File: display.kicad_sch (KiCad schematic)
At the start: 40 parts, among them J301 ConnectorLCDFrontLight, J302 FPC24(0.5MM), J303 FPC10(0.5MM), Q301 2N7002, Q302 2N7002, Q303 AO3401A

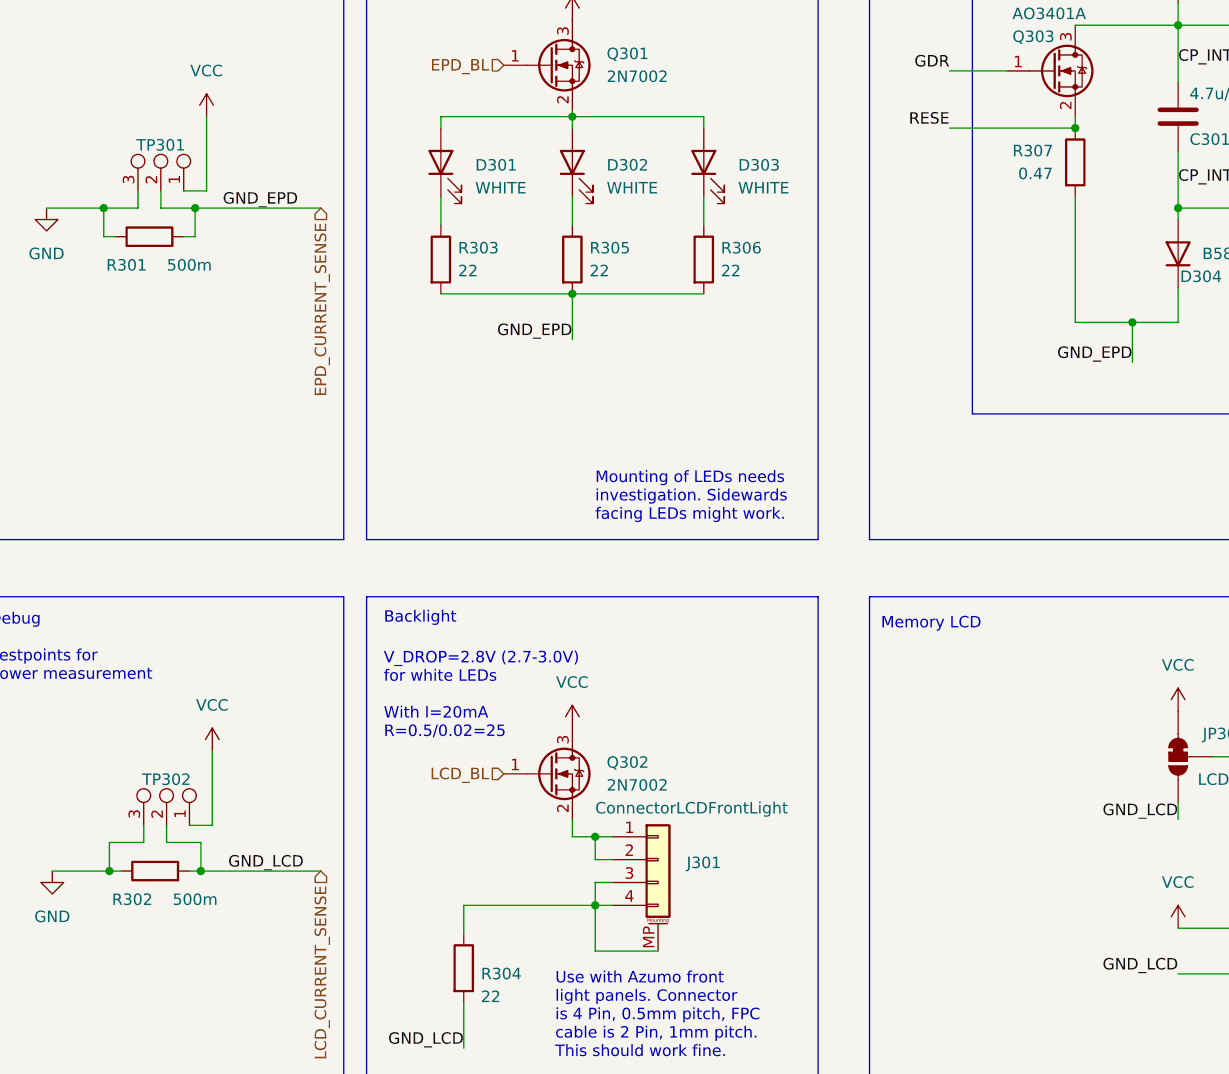
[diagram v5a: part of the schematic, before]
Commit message: Schematic: BOM consolidation and JLCPCB part no annotation
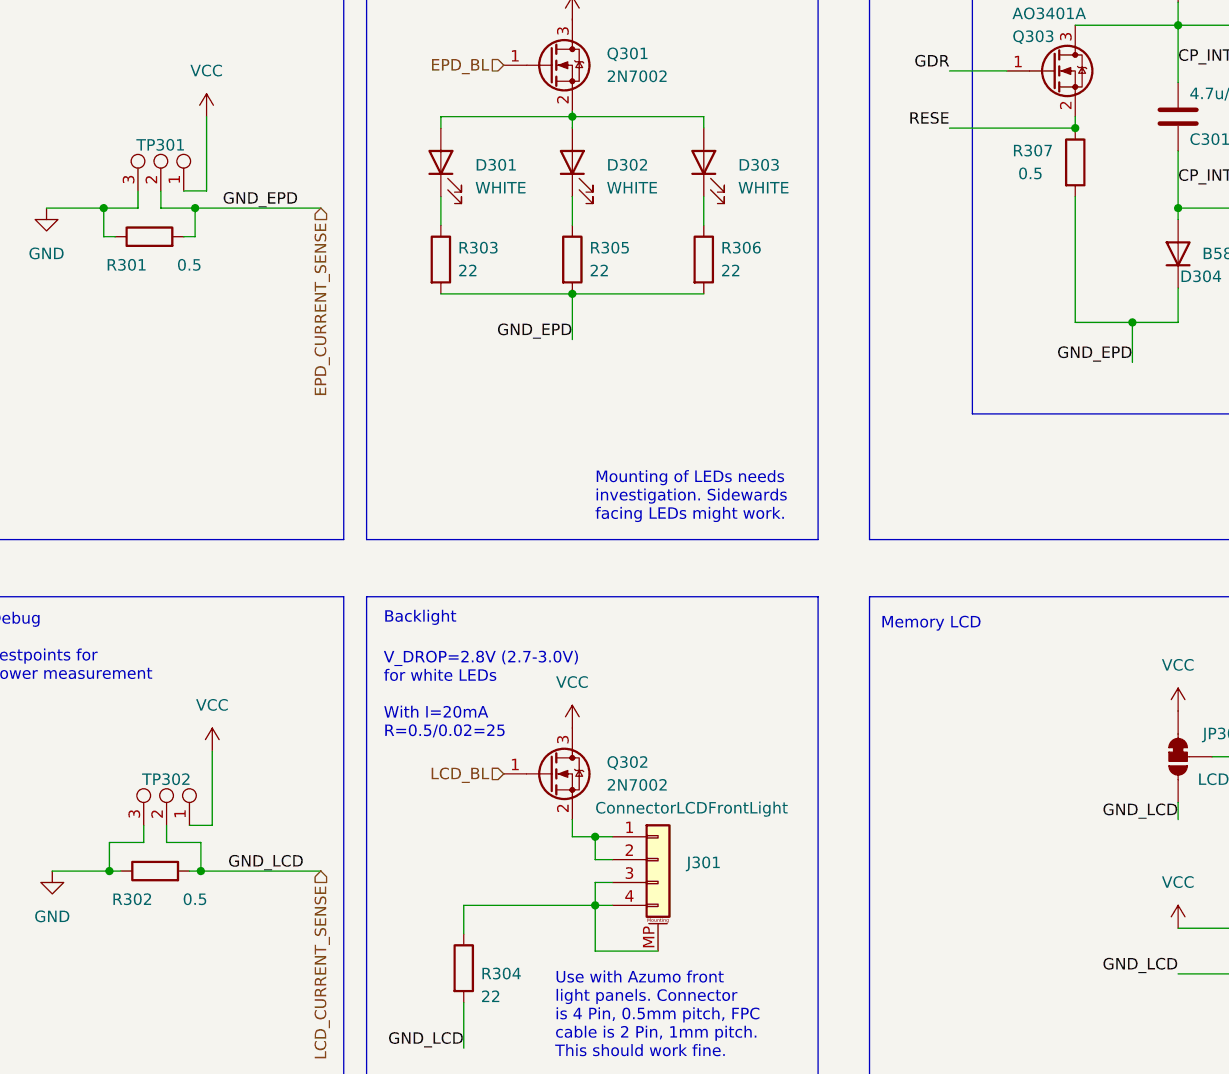
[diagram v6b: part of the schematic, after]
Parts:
- C302, C304, C305, C306, C307, C308, C309, C310, C311, C312: LCSC (none) -> C15849
- C303: LCSC (none) -> C14663
- R301, R302: value 500m -> 0.5; LCSC C25271 -> C28319
- R303, R304, R305, R306: LCSC (none) -> C23345
- R307: value 0.47 -> 0.5; footprint Resistor_SMD:R_0603_1608Metric -> Resistor_SMD:R_0805_2012Metric; LCSC (none) -> C28319
- R308: LCSC (none) -> C25803
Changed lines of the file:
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@@
+      (effects (font (size 1.27 1.27)) hide)
+    )
+    (property "LCSC" "C15849" (id 4) (at 204.47 88.9 0)
       (effects (font (size 1.27 1.27)) hide)
     )
@@
       (effects (font (size 1.27 1.27)) hide)
     )
+    (property "LCSC" "C14663" (id 4) (at 203.2 34.29 0)
+      (effects (font (size 1.27 1.27)) hide)
+    )
     (pin "1")
     (pin "2")
@@
     )
     (property "Datasheet" "~" (id 3) (at 215.265 148.59 0)
+      (effects (font (size 1.27 1.27)) hide)
+    )
+    (property "LCSC" "C15849" (id 4) (at 215.265 148.59 0)
       (effects (font (size 1.27 1.27)) hide)
     )
@@
       (effects (font (size 1.27 1.27)) hide)
     )
+    (property "LCSC" "C15849" (id 4) (at 227.33 40.64 0)
+      (effects (font (size 1.27 1.27)) hide)
+    )
     (pin "1")
     (pin "2")
@@
       (effects (font (size 1.27 1.27)) hide)
     )
+    (property "LCSC" "C15849" (id 4) (at 224.79 88.9 0)
+      (effects (font (size 1.27 1.27)) hide)
+    )
     (pin "1")
     (pin "2")
@@
     )
     (property "Datasheet" "~" (id 3) (at 209.55 88.9 0)
+      (effects (font (size 1.27 1.27)) hide)
+    )
+    (property "LCSC" "C15849" (id 4) (at 209.55 88.9 0)
       (effects (font (size 1.27 1.27)) hide)
     )
@@
       (effects (font (size 1.27 1.27)) hide)
     )
+    (property "LCSC" "C23345" (id 4) (at 92.71 73.025 0)
+      (effects (font (size 1.27 1.27)) hide)
+    )
     (pin "1")
     (pin "2")
@@
     )
     (property "Datasheet" "~" (id 3) (at 80.645 151.765 0)
+      (effects (font (size 1.27 1.27)) hide)
+    )
+    (property "LCSC" "C23345" (id 4) (at 80.645 151.765 0)
       (effects (font (size 1.27 1.27)) hide)
     )
@@
       (effects (font (size 1.27 1.27)) hide)
     )
+    (property "LCSC" "C23345" (id 4) (at 78.105 73.025 0)
+      (effects (font (size 1.27 1.27)) hide)
+    )
     (pin "1")
     (pin "2")
@@
     )
     (property "Datasheet" "~" (id 3) (at 229.87 88.9 0)
+      (effects (font (size 1.27 1.27)) hide)
+    )
+    (property "LCSC" "C15849" (id 4) (at 229.87 88.9 0)
       (effects (font (size 1.27 1.27)) hide)
     )
@@
       (effects (font (size 1.27 1.27)) hide)
     )
+    (property "LCSC" "C15849" (id 4) (at 201.93 148.59 0)
+      (effects (font (size 1.27 1.27)) hide)
+    )
     (pin "1")
     (pin "2")
@@
       (effects (font (size 1.27 1.27)) hide)
     )
+    (property "LCSC" "C15849" (id 4) (at 214.63 88.9 0)
+      (effects (font (size 1.27 1.27)) hide)
+    )
     (pin "1")
     (pin "2")
@@
       (effects (font (size 1.27 1.27)) (justify left))
     )
-    (property "Value" "0.47" (id 1) (at 142.24 63.5 0)
-      (effects (font (size 1.27 1.27)) (justify left))
-    )
-    (property "Footprint" "Resistor_SMD:R_0603_1608Metric" (id 2) (at 146.812 62.23 90)
+    (property "Value" "0.5" (id 1) (at 142.24 63.5 0)
+      (effects (font (size 1.27 1.27)) (justify left))
+    )
+    (property "Footprint" "Resistor_SMD:R_0805_2012Metric" (id 2) (at 146.812 62.23 90)
       (effects (font (size 1.27 1.27)) hide)
     )
     (property "Datasheet" "~" (id 3) (at 148.59 62.23 0)
+      (effects (font (size 1.27 1.27)) hide)
+    )
+    (property "LCSC" "C28319" (id 4) (at 148.59 62.23 0)
       (effects (font (size 1.27 1.27)) hide)
     )
@@
       (effects (font (size 1.27 1.27)) hide)
     )
+    (property "LCSC" "C25803" (id 4) (at 210.82 34.29 0)
+      (effects (font (size 1.27 1.27)) hide)
+    )
     (pin "1")
     (pin "2")
@@
       (effects (font (size 1.27 1.27)) hide)
     )
+    (property "LCSC" "C23345" (id 4) (at 107.315 73.025 0)
+      (effects (font (size 1.27 1.27)) hide)
+    )
     (pin "1")
     (pin "2")
@@
     (in_bom yes) (on_board yes)
     (property "Reference" "R302" (id 0) (at 43.815 144.145 90))
-    (property "Value" "500m" (id 1) (at 50.8 144.145 90))
+    (property "Value" "0.5" (id 1) (at 50.8 144.145 90))
     (property "Footprint" "Resistor_SMD:R_0805_2012Metric" (id 2) (at 46.355 142.748 90)
       (effects (font (size 1.27 1.27)) hide)
@@
       (effects (font (size 1.27 1.27)) hide)
     )
-    (property "LCSC" "C25271" (id 5) (at 46.355 140.97 0)
+    (property "LCSC" "C28319" (id 5) (at 46.355 140.97 0)
       (effects (font (size 1.27 1.27)) hide)
     )
@@
     )
     (property "Datasheet" "~" (id 3) (at 228.6 148.59 0)
+      (effects (font (size 1.27 1.27)) hide)
+    )
+    (property "LCSC" "C15849" (id 4) (at 228.6 148.59 0)
       (effects (font (size 1.27 1.27)) hide)
     )
@@
     (in_bom yes) (on_board yes)
     (property "Reference" "R301" (id 0) (at 43.18 73.66 90))
-    (property "Value" "500m" (id 1) (at 50.165 73.66 90))
+    (property "Value" "0.5" (id 1) (at 50.165 73.66 90))
     (property "Footprint" "Resistor_SMD:R_0805_2012Metric" (id 2) (at 45.72 72.263 90)
       (effects (font (size 1.27 1.27)) hide)
@@
       (effects (font (size 1.27 1.27)) hide)
     )
-    (property "LCSC" "C25271" (id 5) (at 45.72 70.485 0)
+    (property "LCSC" "C28319" (id 5) (at 45.72 70.485 0)
       (effects (font (size 1.27 1.27)) hide)
     )
@@
       (effects (font (size 1.27 1.27)) hide)
     )
+    (property "LCSC" "C15849" (id 4) (at 219.71 88.9 0)
+      (effects (font (size 1.27 1.27)) hide)
+    )
